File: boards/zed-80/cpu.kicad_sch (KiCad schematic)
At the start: 11 parts, among them SW1 SW_Push, U1 GD74LS04, U4 Z84C0010PEC, Y1 7.3728 MHz

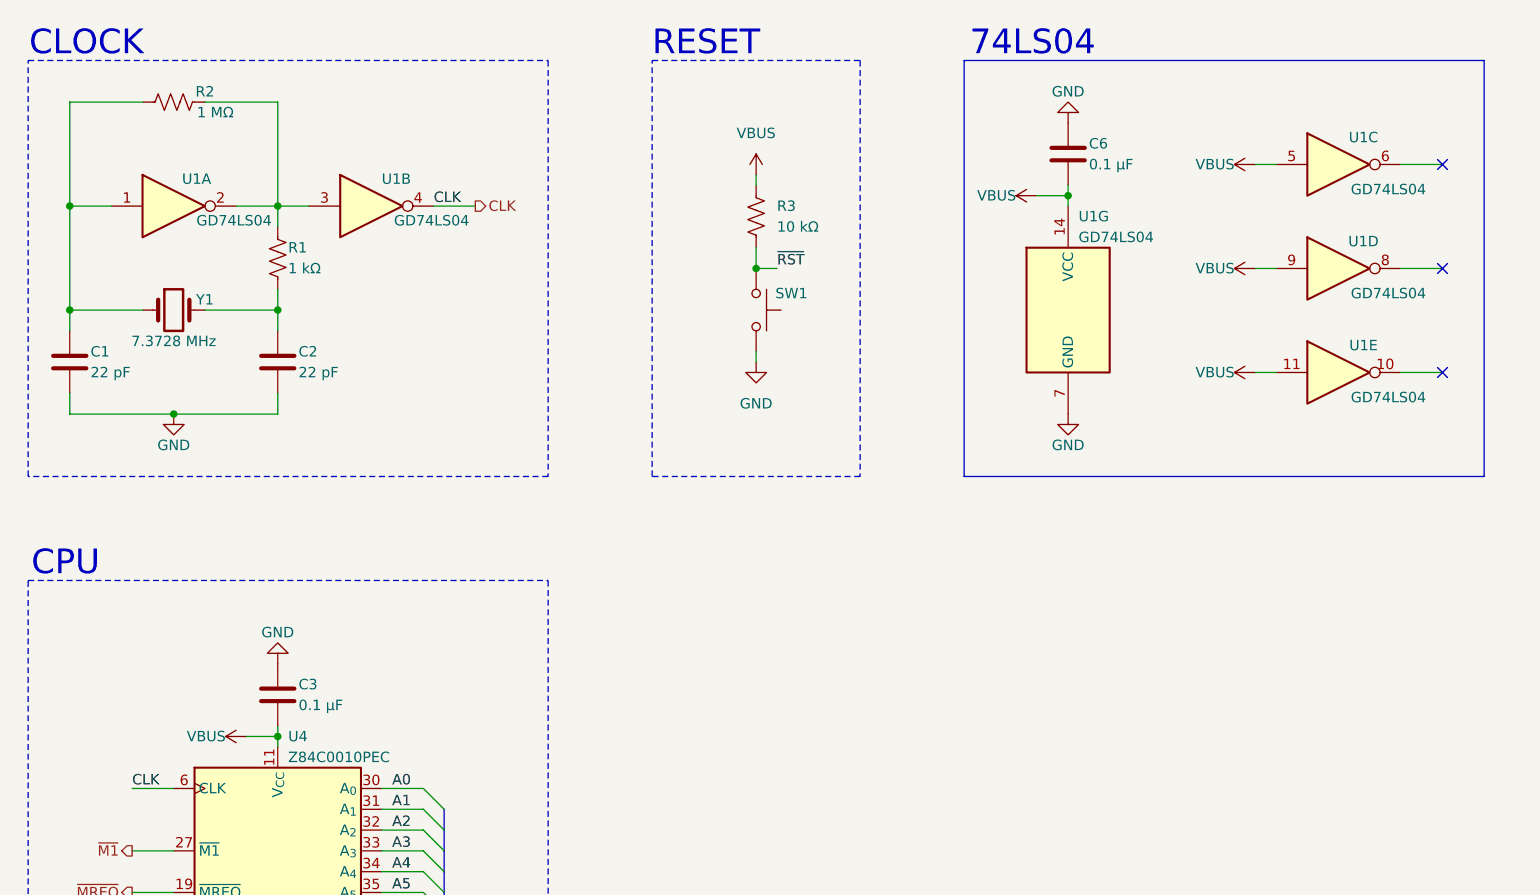
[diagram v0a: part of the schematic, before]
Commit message: Polished schematics and basic PCB setup
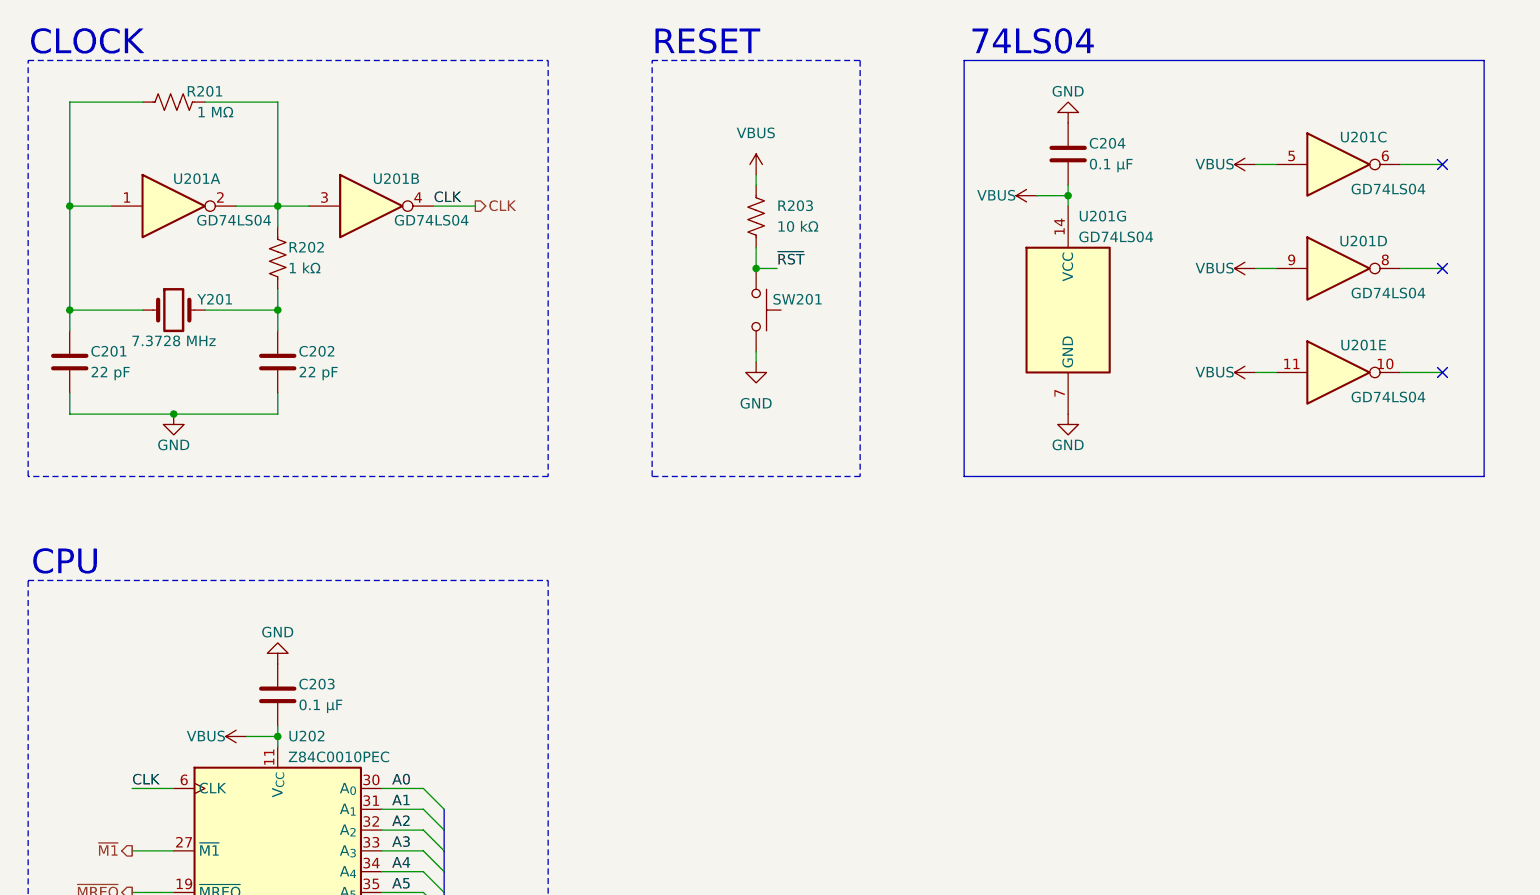
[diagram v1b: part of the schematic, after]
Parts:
- renumbered C1 to C201, C2 to C202, C3 to C203, C6 to C204, R2 to R201, R1 to R202, R3 to R203, SW1 to SW201, U1 to U201, U4 to U202, Y1 to Y201
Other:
- company: (none) -> Dragos Bajanica
- title: (none) -> CPU

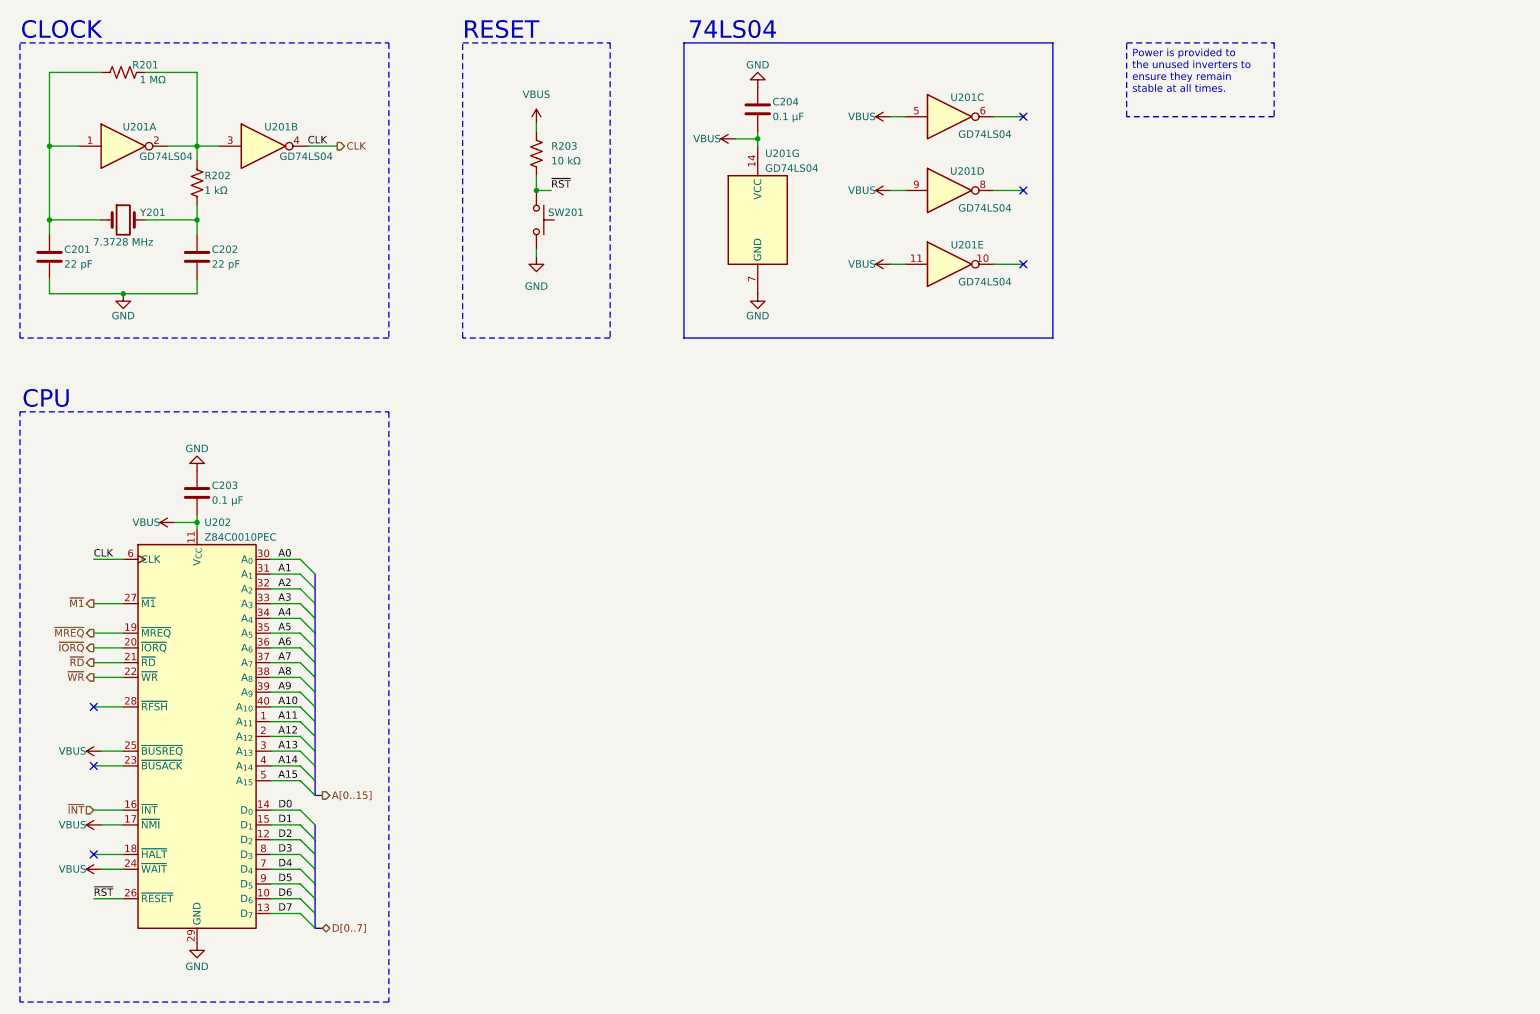
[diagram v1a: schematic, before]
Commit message: New zed-80 revision and initial ROM programmer schematic
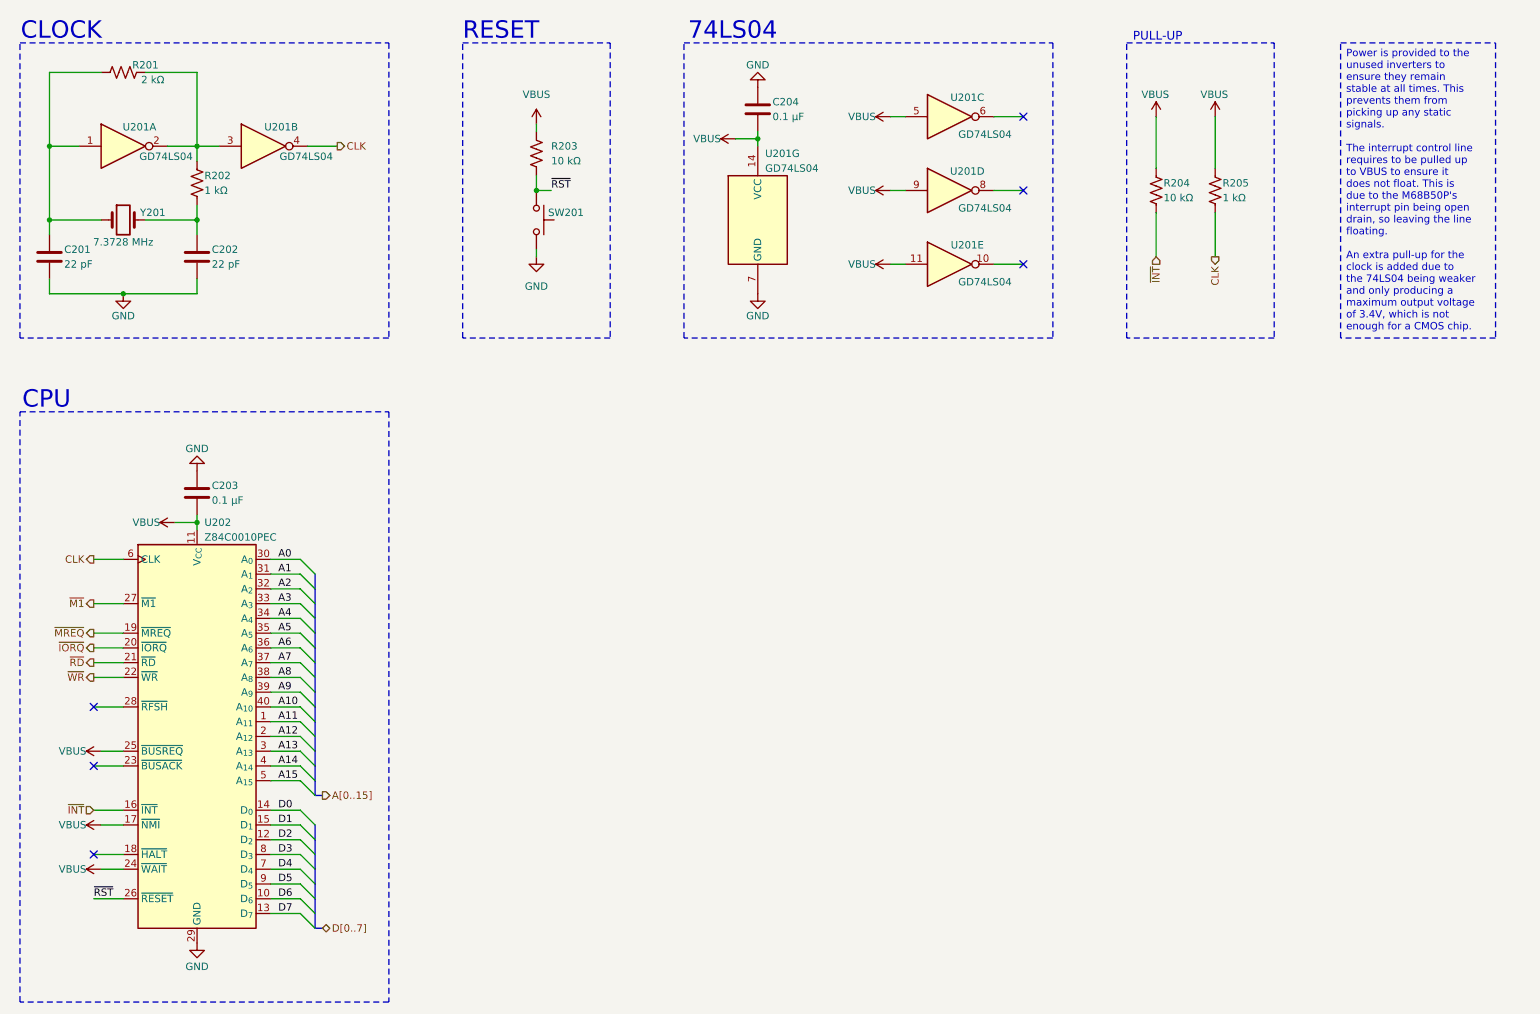
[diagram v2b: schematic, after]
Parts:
- added R204: 10 kΩ, Resistor_THT:R_Axial_DIN0207_L6.3mm_D2.5mm_P7.62mm_Horizontal, symbol Device:R_US
- added R205: 1 kΩ, Resistor_THT:R_Axial_DIN0207_L6.3mm_D2.5mm_P7.62mm_Horizontal, symbol Device:R_US
- R201: value 1 MΩ -> 2 kΩ
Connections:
- net CLK: now also R205.2
- net VBUS: now also R204.1, R205.1
- net ~{INT}: now also R204.2
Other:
- note added: "PULL-UP"

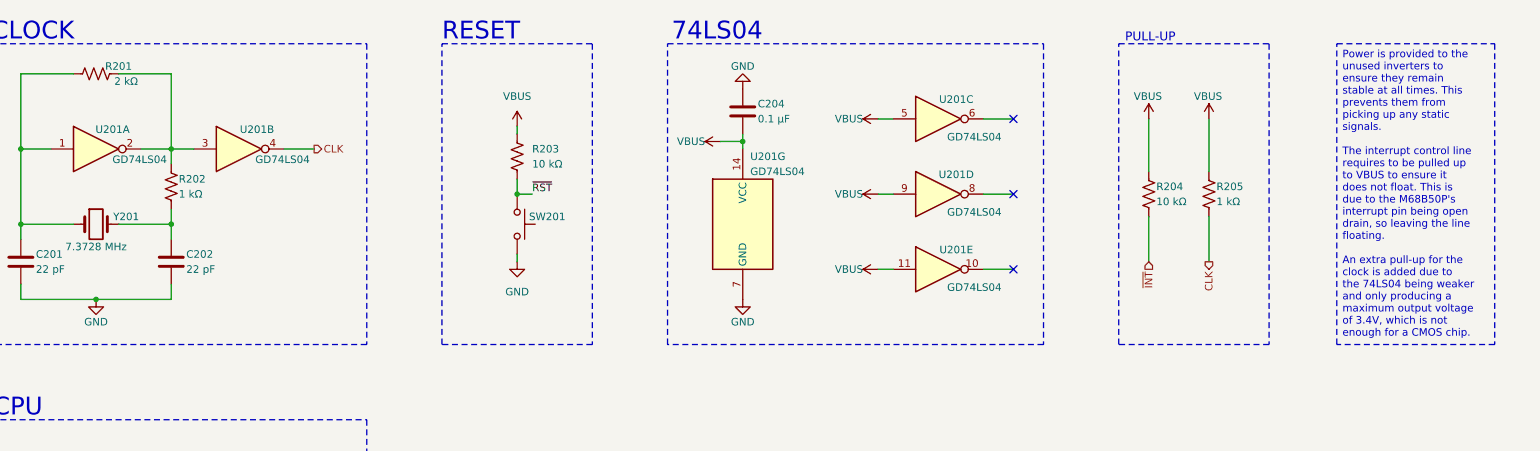
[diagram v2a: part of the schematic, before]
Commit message: Fixed clock oscillator circuit
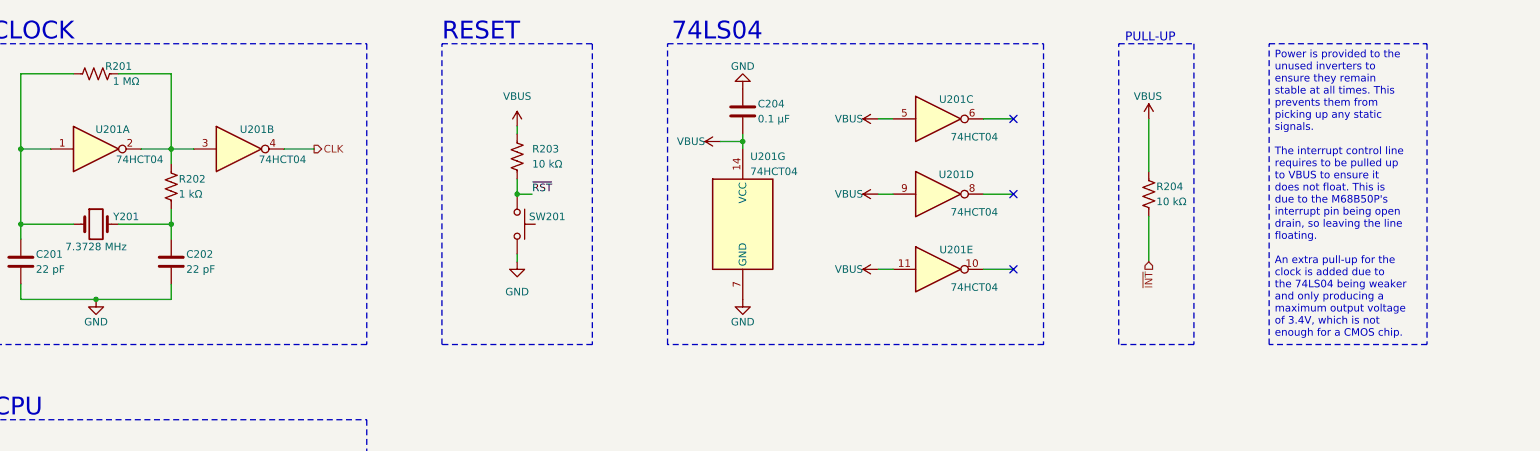
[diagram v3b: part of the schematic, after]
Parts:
- removed R205: 1 kΩ, Resistor_THT:R_Axial_DIN0207_L6.3mm_D2.5mm_P7.62mm_Horizontal, symbol Device:R_US
- R201: value 2 kΩ -> 1 MΩ
- U201: value GD74LS04 -> 74HCT04
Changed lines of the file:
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@@
 	(title_block
 		(title "CPU")
-		(date "2026-01-01")
-		(rev "B")
+		(date "2026-03-17")
+		(rev "C")
 		(company "Dragos Bajanica")
 	)
@@
 	(rectangle
 		(start 215.9 25.4)
-		(end 241.3 76.2)
+		(end 228.6 76.2)
 		(stroke
 			(width 0)
@@
 	(text_box "Power is provided to the unused inverters to ensure they remain stable at all times. This prevents them from picking up any static signals.\n\nThe interrupt control line requires to be pulled up to VBUS to ensure it does not float. This is due to the M68B50P's interrupt pin being open drain, so leaving the line floating.\n\nAn extra pull-up for the clock is added due to the 74LS04 being weaker and only producing a maximum output voltage of 3.4V, which is not enough for a CMOS chip. "
 		(exclude_from_sim no)
-		(at 252.73 25.4 0)
+		(at 241.3 25.4 0)
 		(size 26.67 50.8)
 		(margins 0.9525 0.9525 0.9525 0.9525)
@@
 	(wire
 		(pts
-			(xy 231.14 38.1) (xy 231.14 46.99)
-		)
-		(stroke
-			(width 0)
-			(type default)
-		)
-	)
-	(wire
-		(pts
 			(xy 175.26 50.8) (xy 177.8 50.8)
 		)
@@
 		)
 	)
-	(wire
-		(pts
-			(xy 231.14 54.61) (xy 231.14 62.23)
-		)
-		(stroke
-			(width 0)
-			(type default)
-		)
-	)
 	(label "~{RST}"
 		(at 38.1 172.72 0)
@@
 		)
 	)
-	(hierarchical_label "CLK"
-		(shape output)
-		(at 231.14 62.23 270)
-		(effects
-			(font
-				(size 1.27 1.27)
-			)
-			(justify right)
-		)
-	)
 	(hierarchical_label "~{M1}"
 		(shape output)
@@
 			)
 		)
-		(property "Value" "GD74LS04"
+		(property "Value" "74HCT04"
 			(at 191.516 41.148 0)
 			(effects
@@
 		)
 		(instances
-			(project ""
+			(project "zed-80"
 				(path "/3141ac47-310a-4fc3-ab78-4d4b51ab76a4/8027ce25-6d64-43c4-92ed-291bb3daa7a1"
 					(reference "#PWR0205")
@@
 		)
 		(instances
-			(project ""
+			(project "zed-80"
 				(path "/3141ac47-310a-4fc3-ab78-4d4b51ab76a4/8027ce25-6d64-43c4-92ed-291bb3daa7a1"
 					(reference "#PWR0206")
@@
 			)
 		)
-		(property "Value" "GD74LS04"
+		(property "Value" "74HCT04"
 			(at 50.546 44.958 0)
 			(effects
@@
 			)
 		)
-		(property "Value" "GD74LS04"
+		(property "Value" "74HCT04"
 			(at 74.676 44.958 0)
 			(effects
@@
 			)
 		)
-		(property "Value" "GD74LS04"
+		(property "Value" "74HCT04"
 			(at 153.67 46.99 0)
 			(effects
@@
 	)
 	(symbol
-		(lib_id "Device:R_US")
-		(at 231.14 50.8 0)
-		(unit 1)
-		(exclude_from_sim no)
-		(in_bom yes)
-		(on_board yes)
-		(dnp no)
-		(property "Reference" "R205"
-			(at 232.41 49.53 0)
-			(effects
-				(font
-					(size 1.27 1.27)
-				)
-				(justify left)
-			)
-		)
-		(property "Value" "1 kΩ"
-			(at 232.41 52.07 0)
-			(effects
-				(font
-					(size 1.27 1.27)
-				)
-				(justify left)
-			)
-		)
-		(property "Footprint" "Resistor_THT:R_Axial_DIN0207_L6.3mm_D2.5mm_P7.62mm_Horizontal"
-			(at 232.156 51.054 90)
-			(effects
-				(font
-					(size 1.27 1.27)
-				)
-				(hide yes)
-			)
-		)
-		(property "Datasheet" "~"
-			(at 231.14 50.8 0)
-			(effects
-				(font
-					(size 1.27 1.27)
-				)
-				(hide yes)
-			)
-		)
-		(property "Description" "Resistor, US symbol"
-			(at 231.14 50.8 0)
-			(effects
-				(font
-					(size 1.27 1.27)
-				)
-				(hide yes)
-			)
-		)
-		(pin "1"
-		)
-		(pin "2"
-		)
-		(instances
-			(project "zed-80"
-				(path "/3141ac47-310a-4fc3-ab78-4d4b51ab76a4/8027ce25-6d64-43c4-92ed-291bb3daa7a1"
-					(reference "R205")
-					(unit 1)
-				)
-			)
-		)
-	)
-	(symbol
 		(lib_id "power:GND")
 		(at 114.3 62.23 0)
@@
 			)
 		)
-		(property "Value" "GD74LS04"
+		(property "Value" "74HCT04"
 			(at 191.516 53.848 0)
 			(effects
@@
 			)
 		)
-		(property "Value" "2 kΩ"
+		(property "Value" "1 MΩ"
 			(at 48.26 31.75 90)
 			(effects
@@
 	(symbol
 		(lib_id "power:VBUS")
-		(at 231.14 38.1 0)
-		(unit 1)
-		(exclude_from_sim no)
-		(in_bom yes)
-		(on_board yes)
-		(dnp no)
-		(property "Reference" "#PWR0217"
-			(at 231.14 41.91 0)
-			(effects
-				(font
-					(size 1.27 1.27)
-				)
-				(hide yes)
-			)
-		)
-		(property "Value" "VBUS"
-			(at 228.6 34.29 0)
-			(effects
-				(font
-					(size 1.27 1.27)
-				)
-				(justify left)
-			)
-		)
-		(property "Footprint" ""
-			(at 231.14 38.1 0)
-			(effects
-				(font
-					(size 1.27 1.27)
-				)
-				(hide yes)
-			)
-		)
-		(property "Datasheet" ""
-			(at 231.14 38.1 0)
-			(effects
-				(font
-					(size 1.27 1.27)
-				)
-				(hide yes)
-			)
-		)
-		(property "Description" "Power symbol creates a global label with name \"VBUS\""
-			(at 231.14 38.1 0)
-			(effects
-				(font
-					(size 1.27 1.27)
-				)
-				(hide yes)
-			)
-		)
-		(pin "1"
-		)
-		(instances
-			(project "zed-80"
-				(path "/3141ac47-310a-4fc3-ab78-4d4b51ab76a4/8027ce25-6d64-43c4-92ed-291bb3daa7a1"
-					(reference "#PWR0217")
-					(unit 1)
-				)
-			)
-		)
-	)
-	(symbol
-		(lib_id "power:VBUS")
 		(at 175.26 50.8 90)
 		(unit 1)
@@
 			)
 		)
-		(property "Value" "GD74LS04"
+		(property "Value" "74HCT04"
 			(at 191.516 66.548 0)
 			(effects

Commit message: Small tweaks
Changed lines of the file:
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@@
 	(title_block
 		(title "CPU")
-		(date "2026-03-17")
+		(date "2026-03-20")
 		(rev "C")
 		(company "Dragos Bajanica")
@@
 		)
 	)
-	(text_box "Power is provided to the unused inverters to ensure they remain stable at all times. This prevents them from picking up any static signals.\n\nThe interrupt control line requires to be pulled up to VBUS to ensure it does not float. This is due to the M68B50P's interrupt pin being open drain, so leaving the line floating.\n\nAn extra pull-up for the clock is added due to the 74LS04 being weaker and only producing a maximum output voltage of 3.4V, which is not enough for a CMOS chip. "
+	(text_box "Power is provided to the unused inverters to ensure they remain stable at all times. This prevents them from picking up any static signals.\n\nThe interrupt control line requires to be pulled up to VBUS to ensure it does not float. This is due to the M68B50P's interrupt pin being open drain, so leaving the line floating. "
 		(exclude_from_sim no)
 		(at 241.3 25.4 0)
